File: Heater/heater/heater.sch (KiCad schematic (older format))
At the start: 10 parts, among them J1 , Q1 IRF7401TRPBF

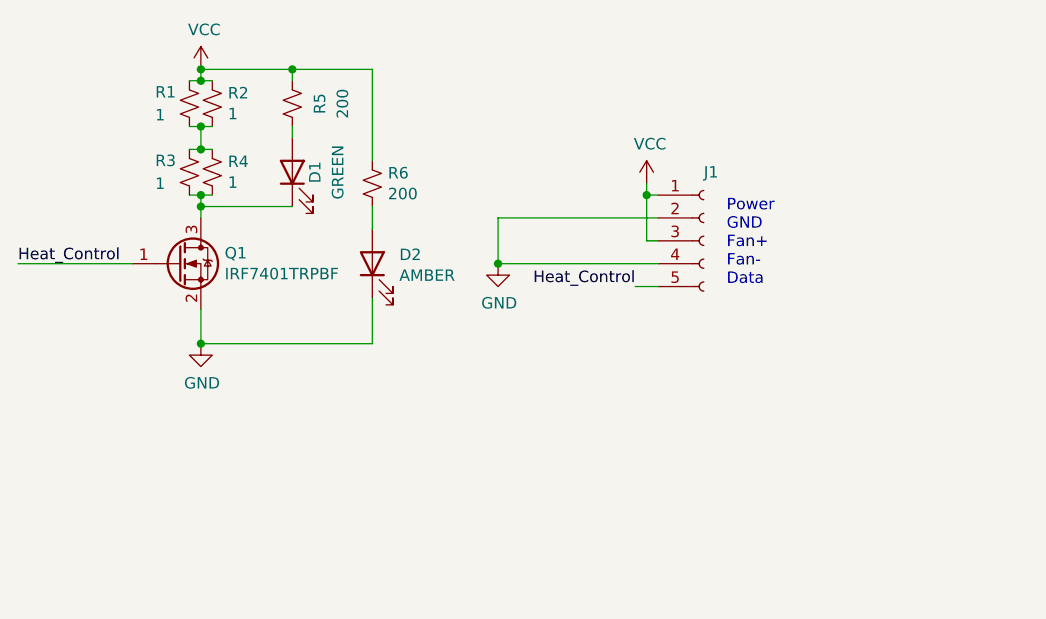
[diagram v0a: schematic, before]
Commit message: update heater pcb
Heater pcb now includes 12V for fan, and a FET to switch the fans on and off
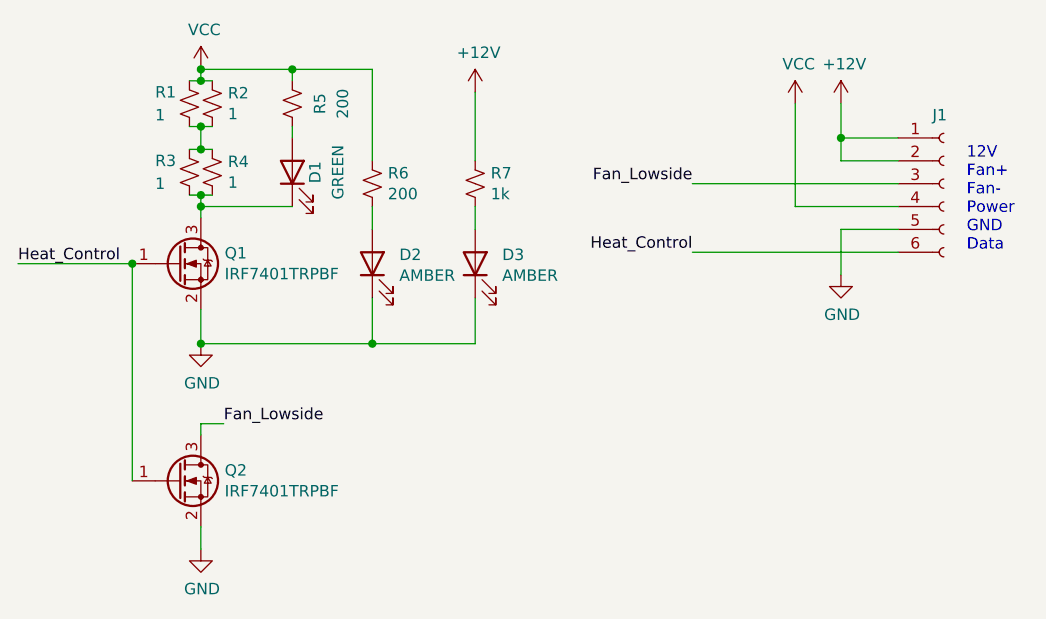
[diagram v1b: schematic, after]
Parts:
- removed J1: (no value), TerminalBlock_Phoenix:TerminalBlock_Phoenix_MKDS-1,5-5_1x05_P5.00mm_Horizontal, symbol Connector:Conn_01x05_Female
- added D3: AMBER, LED_SMD:LED_0805_2012Metric_Pad1.15x1.40mm_HandSolder, symbol Device:LED
- added J1: (no value), TerminalBlock_Phoenix:TerminalBlock_Phoenix_MKDS-1,5-6_1x06_P5.00mm_Horizontal, symbol Connector:Conn_01x06_Female
- added Q2: IRF7401TRPBF, Package_SO:SO-8_3.9x4.9mm_P1.27mm, symbol Device:Q_NMOS_GSD
- added R7: 1k, Resistor_SMD:R_0805_2012Metric_Pad1.15x1.40mm_HandSolder, symbol Device:R_Small_US
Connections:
- net GND: now also D3.1 (K), J1.5 (Pin_5), Q2.2 (S)
- net Heat_Control: now also J1.6 (Pin_6), Q2.1 (G)
- net VCC: now also J1.4 (Pin_4)
- new net: D3.2 (A), R7.2
- new net +12V: J1.1 (Pin_1), J1.2 (Pin_2), R7.1
- new net Fan_Lowside: J1.3 (Pin_3), Q2.3 (D)
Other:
- note added: "12V\nFan+\nFan-\nPower\nGND\nData"
- note removed: "Power\nGND\nFan+\nFan-\nData"
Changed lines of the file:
@@
 L power:VCC #PWR0105
 U 1 1 5F81DB25
-P 4150 1700
-F 0 "#PWR0105" H 4150 1550 50  0001 C CNN
-F 1 "VCC" H 4165 1873 50  0000 C CNN
-F 2 "" H 4150 1700 50  0001 C CNN
-F 3 "" H 4150 1700 50  0001 C CNN
-	1    4150 1700
+P 4800 1350
+F 0 "#PWR0105" H 4800 1200 50  0001 C CNN
+F 1 "VCC" H 4815 1523 50  0000 C CNN
+F 2 "" H 4800 1350 50  0001 C CNN
+F 3 "" H 4800 1350 50  0001 C CNN
+	1    4800 1350
 	1    0    0    -1
 $EndComp
@@
 L power:GND #PWR0106
 U 1 1 5F81DE71
-P 3500 2050
-F 0 "#PWR0106" H 3500 1800 50  0001 C CNN
-F 1 "GND" H 3505 1877 50  0000 C CNN
-F 2 "" H 3500 2050 50  0001 C CNN
-F 3 "" H 3500 2050 50  0001 C CNN
-	1    3500 2050
-	1    0    0    -1
-$EndComp
-Text Label 4100 2150 2    50   ~ 0
+P 5000 2100
+F 0 "#PWR0106" H 5000 1850 50  0001 C CNN
+F 1 "GND" H 5005 1927 50  0000 C CNN
+F 2 "" H 5000 2100 50  0001 C CNN
+F 3 "" H 5000 2100 50  0001 C CNN
+	1    5000 2100
+	1    0    0    -1
+$EndComp
+Text Label 4350 2000 2    50   ~ 0
 Heat_Control
 Text Label 1400 2050 0    50   ~ 0
 Heat_Control
-$Comp
-L Connector:Conn_01x05_Female J1
-U 1 1 5F82558B
-P 4400 1950
-F 0 "J1" H 4400 2250 50  0000 L CNN
-F 1 " " H 4428 1885 50  0000 L CNN
-F 2 "TerminalBlock_Phoenix:TerminalBlock_Phoenix_MKDS-1,5-5_1x05_P5.00mm_Horizontal" H 4400 1950 50  0001 C CNN
-F 3 "~" H 4400 1950 50  0001 C CNN
-	1    4400 1950
-	1    0    0    -1
-$EndComp
-Wire Wire Line
-	4200 1750 4150 1750
-Wire Wire Line
-	4150 1750 4150 1700
-Wire Wire Line
-	4200 1950 4150 1950
-Wire Wire Line
-	4150 1950 4150 1750
-Connection ~ 4150 1750
-Wire Wire Line
-	4200 1850 3500 1850
-Wire Wire Line
-	3500 1850 3500 2050
-Wire Wire Line
-	4200 2050 3500 2050
-Connection ~ 3500 2050
-Wire Wire Line
-	4100 2150 4200 2150
-Text Notes 4500 2150 0    50   ~ 0
-Power\nGND\nFan+\nFan-\nData
 $Comp
 L Device:R_Small_US R3
@@
 Wire Wire Line
 	2200 1800 2200 1850
+$Comp
+L power:+12V #PWR0103
+U 1 1 5F889262
+P 5000 1350
+F 0 "#PWR0103" H 5000 1200 50  0001 C CNN
+F 1 "+12V" H 5015 1523 50  0000 C CNN
+F 2 "" H 5000 1350 50  0001 C CNN
+F 3 "" H 5000 1350 50  0001 C CNN
+	1    5000 1350
+	1    0    0    -1
+$EndComp
+Text Notes 5550 2000 0    50   ~ 0
+12V\nFan+\nFan-\nPower\nGND\nData
+Wire Wire Line
+	4800 1350 4800 1800
+Wire Wire Line
+	4800 1800 5250 1800
+Wire Wire Line
+	5250 1600 5000 1600
+Wire Wire Line
+	4350 2000 5250 2000
+Wire Wire Line
+	5250 1700 4350 1700
+Text Label 4350 1700 2    50   ~ 0
+Fan_Lowside
+$Comp
+L Device:Q_NMOS_GSD Q2
+U 1 1 5F89A74A
+P 2100 3000
+F 0 "Q2" H 2304 3046 50  0000 L CNN
+F 1 "IRF7401TRPBF" H 2304 2955 50  0000 L CNN
+F 2 "Package_SO:SO-8_3.9x4.9mm_P1.27mm" H 2300 3100 50  0001 C CNN
+F 3 "~" H 2100 3000 50  0001 C CNN
+	1    2100 3000
+	1    0    0    -1
+$EndComp
+$Comp
+L Connector:Conn_01x06_Female J1
+U 1 1 5F89E31E
+P 5450 1700
+F 0 "J1" H 5400 2000 50  0000 L CNN
+F 1 " " H 5478 1585 50  0000 L CNN
+F 2 "TerminalBlock_Phoenix:TerminalBlock_Phoenix_MKDS-1,5-6_1x06_P5.00mm_Horizontal" H 5450 1700 50  0001 C CNN
+F 3 "~" H 5450 1700 50  0001 C CNN
+	1    5450 1700
+	1    0    0    -1
+$EndComp
+Wire Wire Line
+	5000 1350 5000 1500
+Wire Wire Line
+	5250 1500 5000 1500
+Connection ~ 5000 1500
+Wire Wire Line
+	5000 1500 5000 1600
+Wire Wire Line
+	5250 1900 5000 1900
+Wire Wire Line
+	5000 1900 5000 2100
+Wire Wire Line
+	1900 3000 1900 2050
+Connection ~ 1900 2050
+Wire Wire Line
+	2200 2800 2200 2750
+Wire Wire Line
+	2200 2750 2300 2750
+Text Label 2300 2750 0    50   ~ 0
+Fan_Lowside
+$Comp
+L power:GND #PWR0104
+U 1 1 5F8A33F4
+P 2200 3300
+F 0 "#PWR0104" H 2200 3050 50  0001 C CNN
+F 1 "GND" H 2205 3127 50  0000 C CNN
+F 2 "" H 2200 3300 50  0001 C CNN
+F 3 "" H 2200 3300 50  0001 C CNN
+	1    2200 3300
+	1    0    0    -1
+$EndComp
+Wire Wire Line
+	2200 3200 2200 3300
+$Comp
+L Device:LED D3
+U 1 1 5F89D85A
+P 3400 2050
+F 0 "D3" V 3439 1932 50  0000 R CNN
+F 1 "AMBER" V 3348 1932 50  0000 R CNN
+F 2 "LED_SMD:LED_0805_2012Metric_Pad1.15x1.40mm_HandSolder" H 3400 2050 50  0001 C CNN
+F 3 "~" H 3400 2050 50  0001 C CNN
+	1    3400 2050
+	0    -1   -1   0
+$EndComp
+Wire Wire Line
+	3400 2200 3400 2400
+Wire Wire Line
+	3400 2400 2950 2400
+Connection ~ 2950 2400
+$Comp
+L Device:R_Small_US R7
+U 1 1 5F89E5AE
+P 3400 1700
+F 0 "R7" H 3468 1746 50  0000 L CNN
+F 1 "1k" H 3468 1655 50  0000 L CNN
+F 2 "Resistor_SMD:R_0805_2012Metric_Pad1.15x1.40mm_HandSolder" H 3400 1700 50  0001 C CNN
+F 3 "~" H 3400 1700 50  0001 C CNN
+	1    3400 1700
+	1    0    0    -1
+$EndComp
+Wire Wire Line
+	3400 1900 3400 1800
+Wire Wire Line
+	3400 1300 3400 1600
+$Comp
+L power:+12V #PWR0107
+U 1 1 5F8A0706
+P 3400 1300
+F 0 "#PWR0107" H 3400 1150 50  0001 C CNN
+F 1 "+12V" H 3415 1473 50  0000 C CNN
+F 2 "" H 3400 1300 50  0001 C CNN
+F 3 "" H 3400 1300 50  0001 C CNN
+	1    3400 1300
+	1    0    0    -1
+$EndComp
 $EndSCHEMATC
